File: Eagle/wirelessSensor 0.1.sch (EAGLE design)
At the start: 2 parts, among them U1 HDC1080, U2 PIC16F1823-X_SL

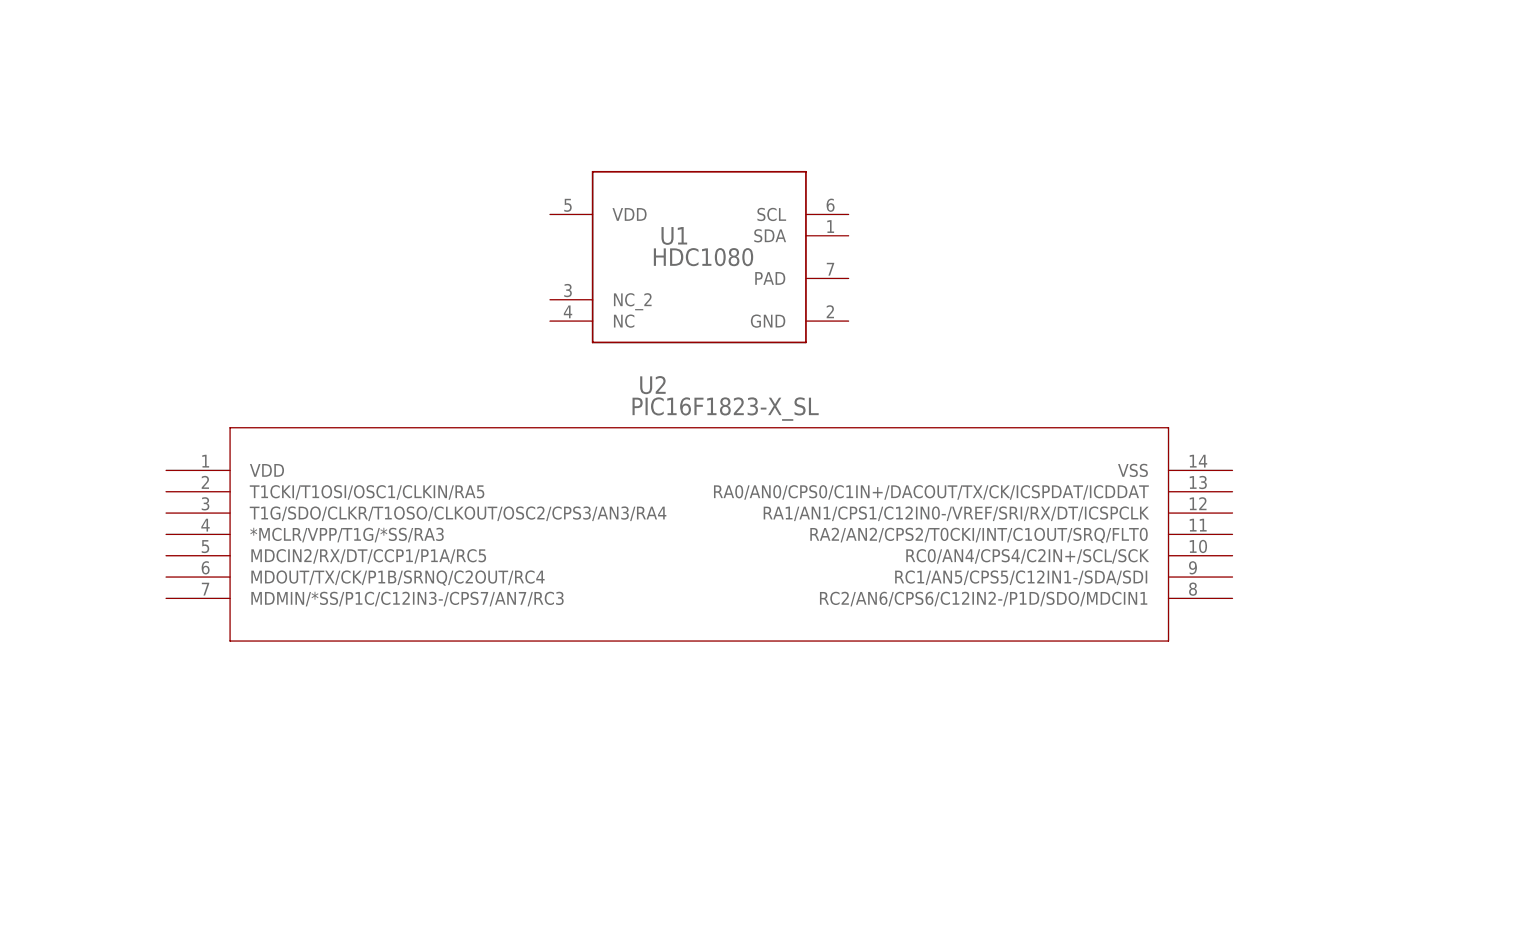
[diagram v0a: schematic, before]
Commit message: Started an Eagle layout and schematic
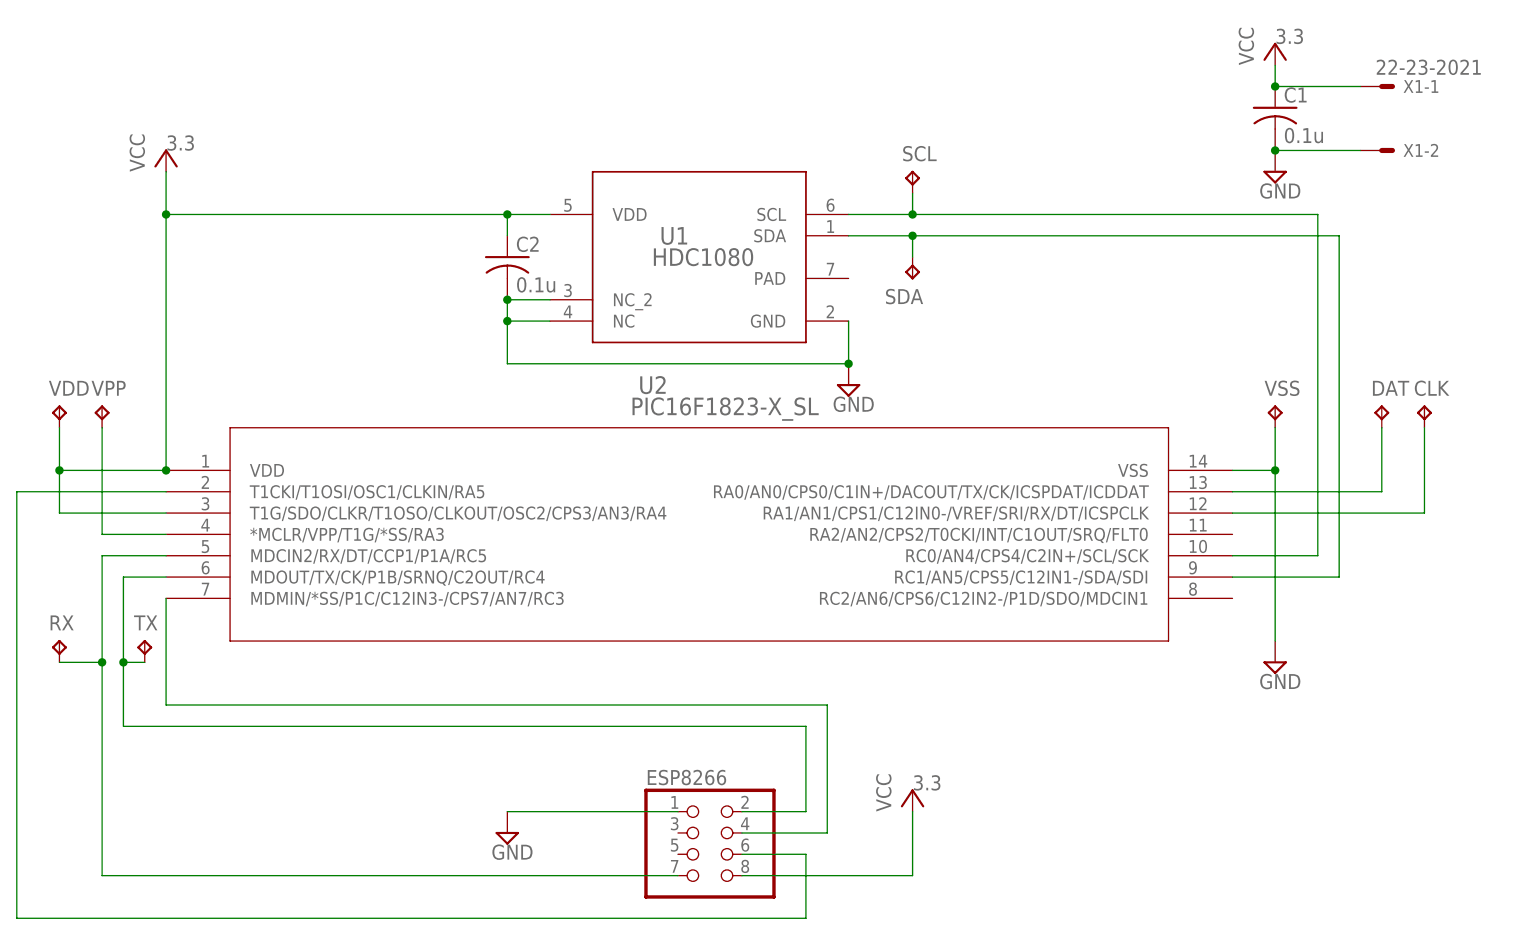
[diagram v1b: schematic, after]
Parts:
- added C1, C2: 0.1u, rcl:C-USC0603
- added CLK, DAT, RX, SCL, SDA, TX, VDD, VPP, VSS: TPB1,27, testpad:TPB1,27
- added ESP8266: (no value), pinhead:PINHD-2X4
- added X1: 22-23-2021, con-molex:22-23-2021
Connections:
- new net GND: C1.2, C2.2, ESP8266.1, U1.GND, U1.NC, U1.NC_2, U2.VSS, VSS.TP, X1-2.S
- new net N$1: ESP8266.2, TX.TP, U2.MDOUT/TX/CK/P1B/SRNQ/C2OUT/RC4
- new net N$2: SCL.TP, U1.SCL, U2.RC0/AN4/CPS4/C2IN+/SCL/SCK
- new net N$3: SDA.TP, U1.SDA, U2.RC1/AN5/CPS5/C12IN1-/SDA/SDI
- new net N$4: U2.*MCLR/VPP/T1G/*SS/RA3, VPP.TP
- new net N$5: DAT.TP, U2.RA0/AN0/CPS0/C1IN+/DACOUT/TX/CK/ICSPDAT/ICDDAT
- new net N$6: CLK.TP, U2.RA1/AN1/CPS1/C12IN0-/VREF/SRI/RX/DT/ICSPCLK
- new net N$7: ESP8266.7, RX.TP, U2.MDCIN2/RX/DT/CCP1/P1A/RC5
- new net N$8: ESP8266.4, U2.MDMIN/*SS/P1C/C12IN3-/CPS7/AN7/RC3
- new net N$9: ESP8266.6, U2.T1CKI/T1OSI/OSC1/CLKIN/RA5
- new net VCC: C1.1, C2.1, ESP8266.8, U1.VDD, U2.T1G/SDO/CLKR/T1OSO/CLKOUT/OSC2/CPS3/AN3/RA4, U2.VDD, VDD.TP, X1-1.S
